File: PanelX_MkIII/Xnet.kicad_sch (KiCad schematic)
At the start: 5 parts, among them U11 MAX485E

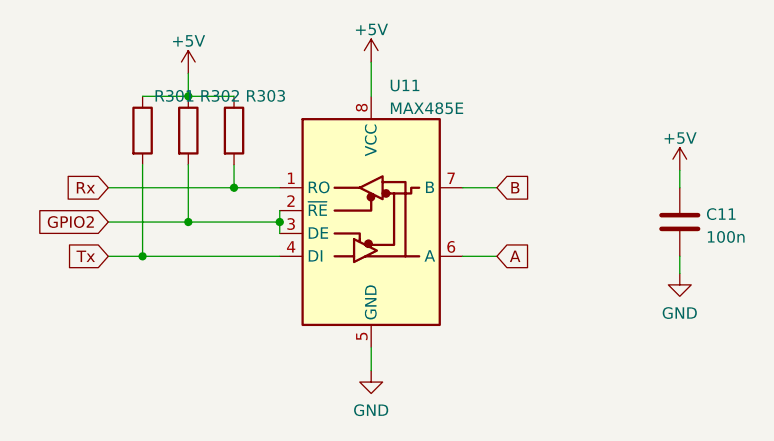
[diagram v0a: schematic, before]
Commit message: added nano project to repo. Must be modular flatcable design. I want to make 2 versions, one with voltage regulator and Xnet and one as I2C slave
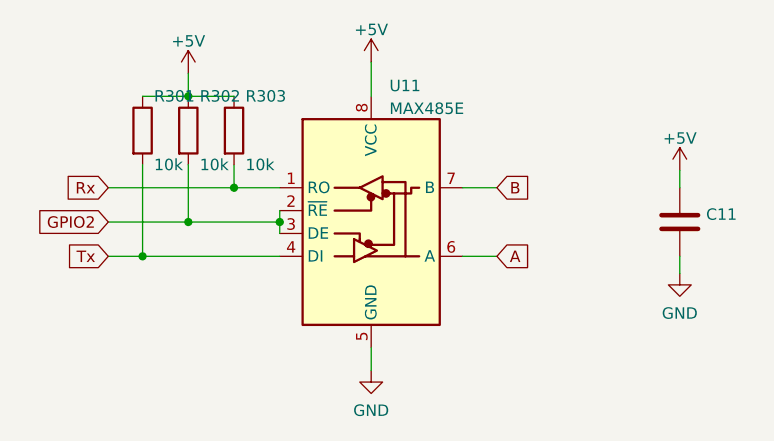
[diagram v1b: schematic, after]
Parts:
- C11: value 100n -> (none); footprint Capacitor_SMD:C_0603_1608Metric_Pad1.08x0.95mm_HandSolder -> (none); JLCPCB Part# (none) -> C14663
- R301, R302, R303: value (none) -> 10k; footprint (none) -> Resistor_SMD:R_0402_1005Metric
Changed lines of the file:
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@@
       (effects (font (size 1.27 1.27)) (justify left))
     )
-    (property "Value" "" (id 1) (at 73.66 82.55 0)
+    (property "Value" "10k" (id 1) (at 73.66 82.55 0)
       (effects (font (size 1.27 1.27)) (justify left))
     )
-    (property "Footprint" "" (id 2) (at 70.612 78.74 90)
+    (property "Footprint" "Resistor_SMD:R_0402_1005Metric" (id 2) (at 70.612 78.74 90)
       (effects (font (size 1.27 1.27)) hide)
     )
@@
       (effects (font (size 1.27 1.27)) (justify left))
     )
-    (property "Value" "" (id 1) (at 78.74 82.55 0)
+    (property "Value" "10k" (id 1) (at 78.74 82.55 0)
       (effects (font (size 1.27 1.27)) (justify left))
     )
-    (property "Footprint" "" (id 2) (at 75.692 78.74 90)
+    (property "Footprint" "Resistor_SMD:R_0402_1005Metric" (id 2) (at 75.692 78.74 90)
       (effects (font (size 1.27 1.27)) hide)
     )
@@
       (effects (font (size 1.27 1.27)) (justify left))
     )
-    (property "Value" "100n" (id 1) (at 129.921 90.6022 0)
+    (property "Value" "" (id 1) (at 129.921 90.6022 0)
       (effects (font (size 1.27 1.27)) (justify left))
     )
-    (property "Footprint" "Capacitor_SMD:C_0603_1608Metric_Pad1.08x0.95mm_HandSolder" (id 2) (at 127.9652 92.71 0)
+    (property "Footprint" "" (id 2) (at 127.9652 92.71 0)
       (effects (font (size 1.27 1.27)) hide)
     )
     (property "Datasheet" "~" (id 3) (at 127 88.9 0)
+      (effects (font (size 1.27 1.27)) hide)
+    )
+    (property "JLCPCB Part#" "C14663" (id 4) (at 127 88.9 0)
       (effects (font (size 1.27 1.27)) hide)
     )
@@
       (effects (font (size 1.27 1.27)) (justify left))
     )
-    (property "Value" "" (id 1) (at 68.58 82.55 0)
+    (property "Value" "10k" (id 1) (at 68.58 82.55 0)
       (effects (font (size 1.27 1.27)) (justify left))
     )
-    (property "Footprint" "" (id 2) (at 65.532 78.74 90)
+    (property "Footprint" "Resistor_SMD:R_0402_1005Metric" (id 2) (at 65.532 78.74 90)
       (effects (font (size 1.27 1.27)) hide)
     )
